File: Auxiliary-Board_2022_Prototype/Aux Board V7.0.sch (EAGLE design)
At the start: 40 parts, among them CON11 1X01, CON12 1X01, CON13 1X01, CON14 1X01, CON15 1X01, CON16 1X01, CON17 1X01, CON18 1X01, CON5 1X01, CON8 1X01

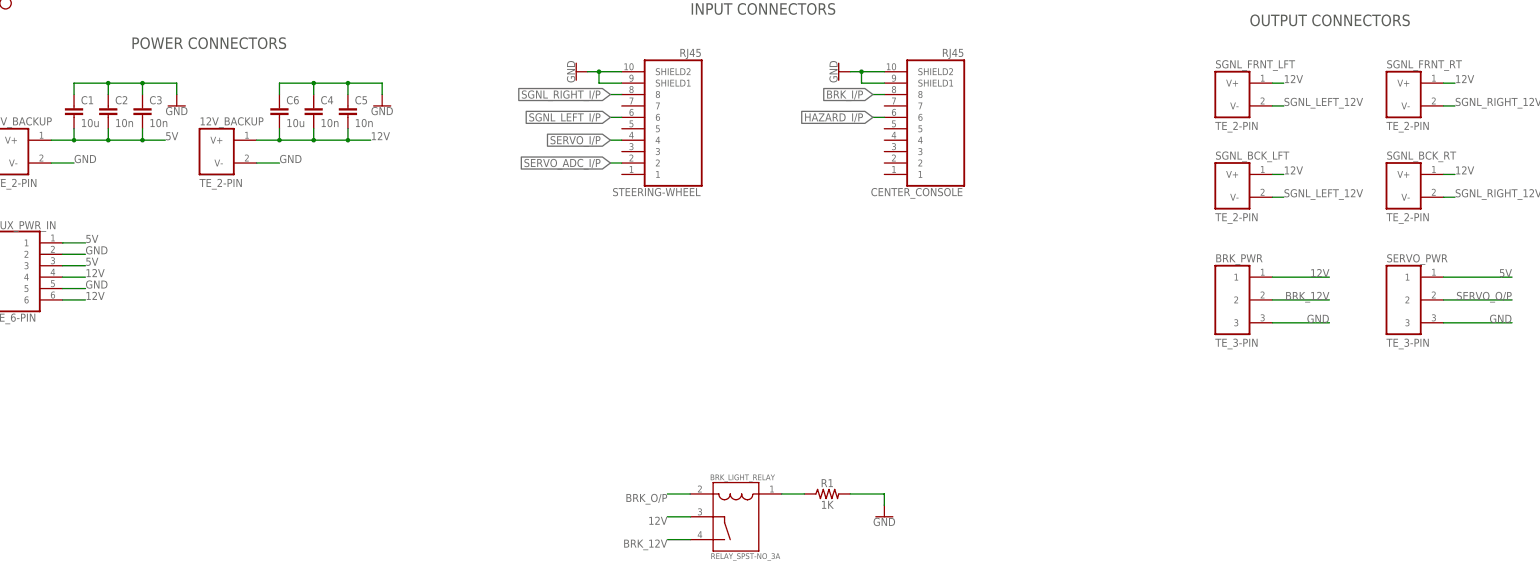
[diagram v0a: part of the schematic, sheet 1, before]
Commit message: feat: rework board, add pwr LEDs, add decoupling caps, add flyback diode
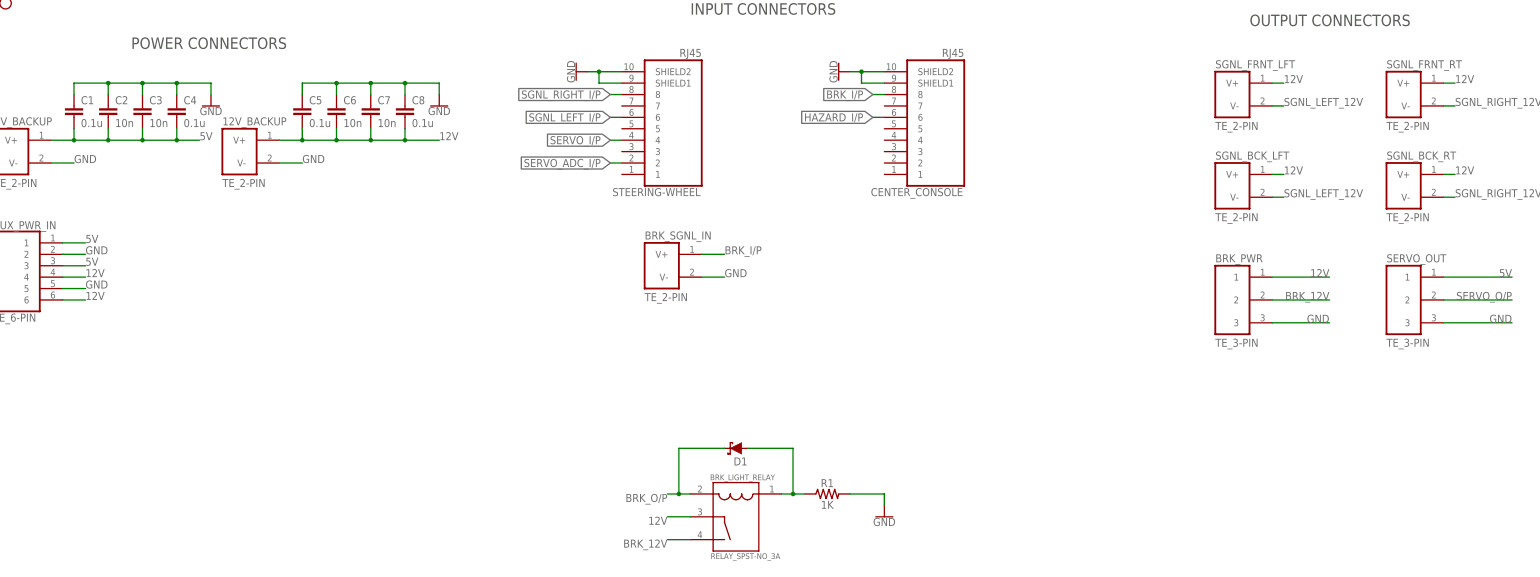
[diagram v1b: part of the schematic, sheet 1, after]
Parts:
- added BRK_SGNL_IN: TE_2-PIN, EcoCar-Connectors:TE_2-PIN
- added C7: 10n, EcoCar-Passives:CAPACITOR_0805
- added C8: 0.1u, EcoCar-Passives:CAPACITOR_0805
- added D1: (no value), EcoCar-Discrete-Semiconductors:DIODE_SCHOTTKY_DO-214AA
- added LED1: (no value), EcoCar-Discrete-Semiconductors:LED_0805
- added R2: 2K, EcoCar-Passives:RESISTOR_0805
- C1: value 10u -> 0.1u
- C4, C5: value 10n -> 0.1u
- C6: value 10u -> 10n
- renumbered SERVO_PWR to SERVO_OUT
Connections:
- new net N$8: LED1.A, R2.1
- net 12V: now also C7.2, C8.2; no longer C4.2
- net 5V: now also C4.2, R2.2
- net BRK_I/P: now also BRK_SGNL_IN.V+, MCU_328P2.PD2(INT0); no longer MCU_328P2.PC1(ADC1)
- net BRK_O/P: now also D1.C
- net GND: now also BRK_SGNL_IN.V-, C7.1, C8.1, LED1.C
- net N$1: now also D1.A
- net SERVO_I/P: now also MCU_328P2.PC1(ADC1); no longer MCU_328P2.PD2(INT0)
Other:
- moved on the sheet: 12V_BACKUP, AVCC_JMP, C4, C5, C6

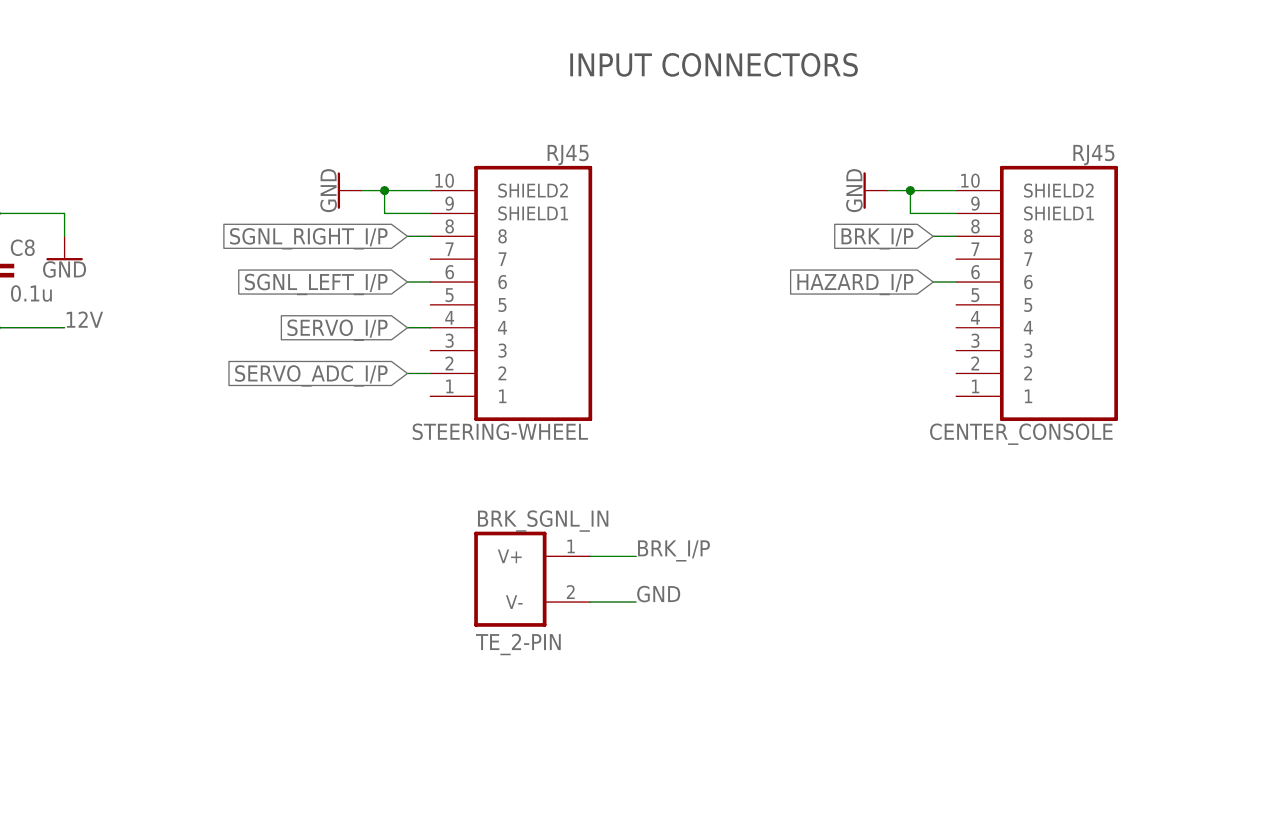
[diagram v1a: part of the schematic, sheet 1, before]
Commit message: feat: add RS232 partially, change inputs to one RJ45 port
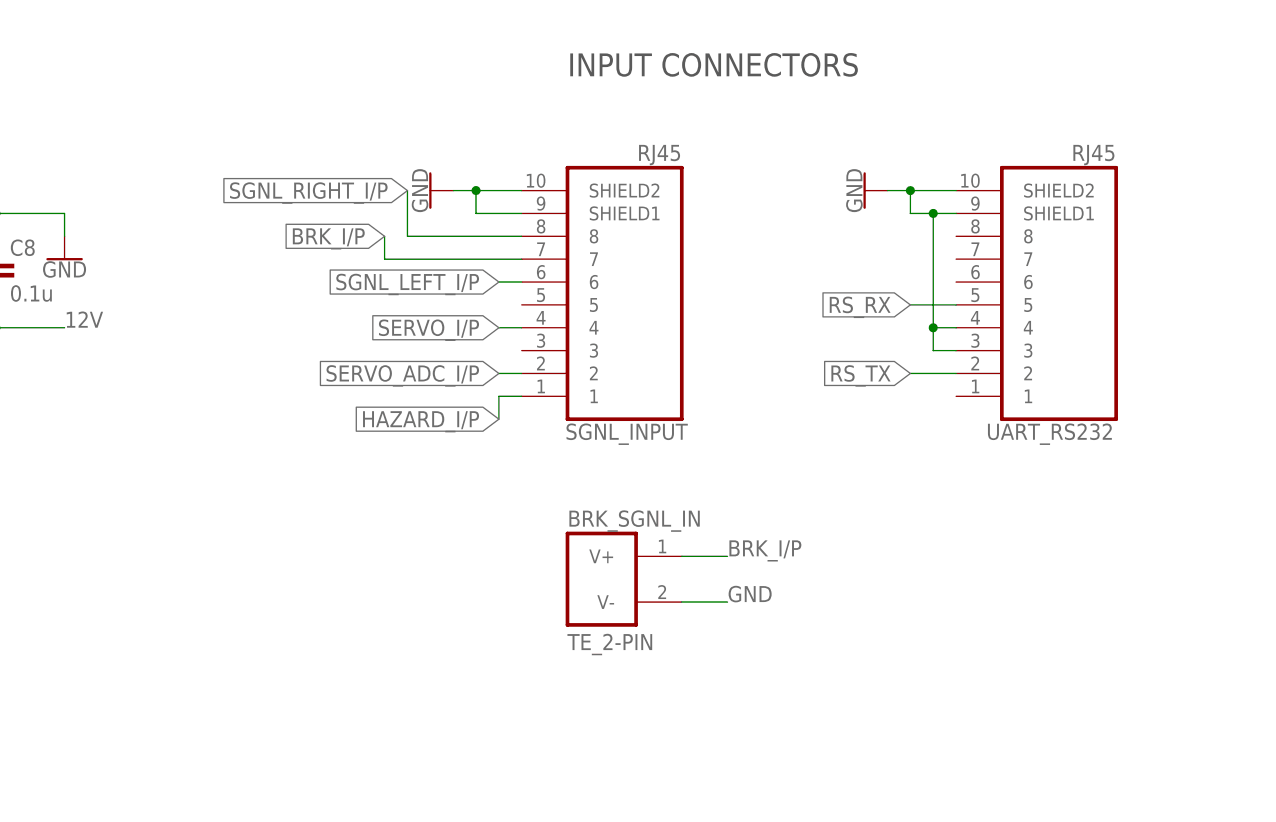
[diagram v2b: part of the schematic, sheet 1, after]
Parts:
- removed STEERING-WHEEL: RJ45, EcoCar-Connectors:RJ45
- added SGNL_INPUT: RJ45, EcoCar-Connectors:RJ45
- renumbered CENTER_CONSOLE to UART_RS232
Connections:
- new net RS_RX: UART_RS232.5
- new net RS_TX: UART_RS232.2
- net BRK_I/P: now also SGNL_INPUT.7; no longer UART_RS232.8
- net GND: now also SGNL_INPUT.SHIELD1, SGNL_INPUT.SHIELD2, UART_RS232.3, UART_RS232.4; no longer STEERING-WHEEL.SHIELD1, STEERING-WHEEL.SHIELD2
- net HAZARD_I/P: now also SGNL_INPUT.1; no longer UART_RS232.6
- net SERVO_ADC_I/P: now also SGNL_INPUT.2; no longer STEERING-WHEEL.2
- net SERVO_I/P: now also SGNL_INPUT.4; no longer STEERING-WHEEL.4
- net SERVO_O/P: now also MCU_328P2.PC5(ADC5/SCL)
- net SGNL_LEFT_I/P: now also SGNL_INPUT.6; no longer STEERING-WHEEL.6
- net SGNL_RIGHT_I/P: now also SGNL_INPUT.8; no longer STEERING-WHEEL.8
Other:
- moved on the sheet: BRK_SGNL_IN

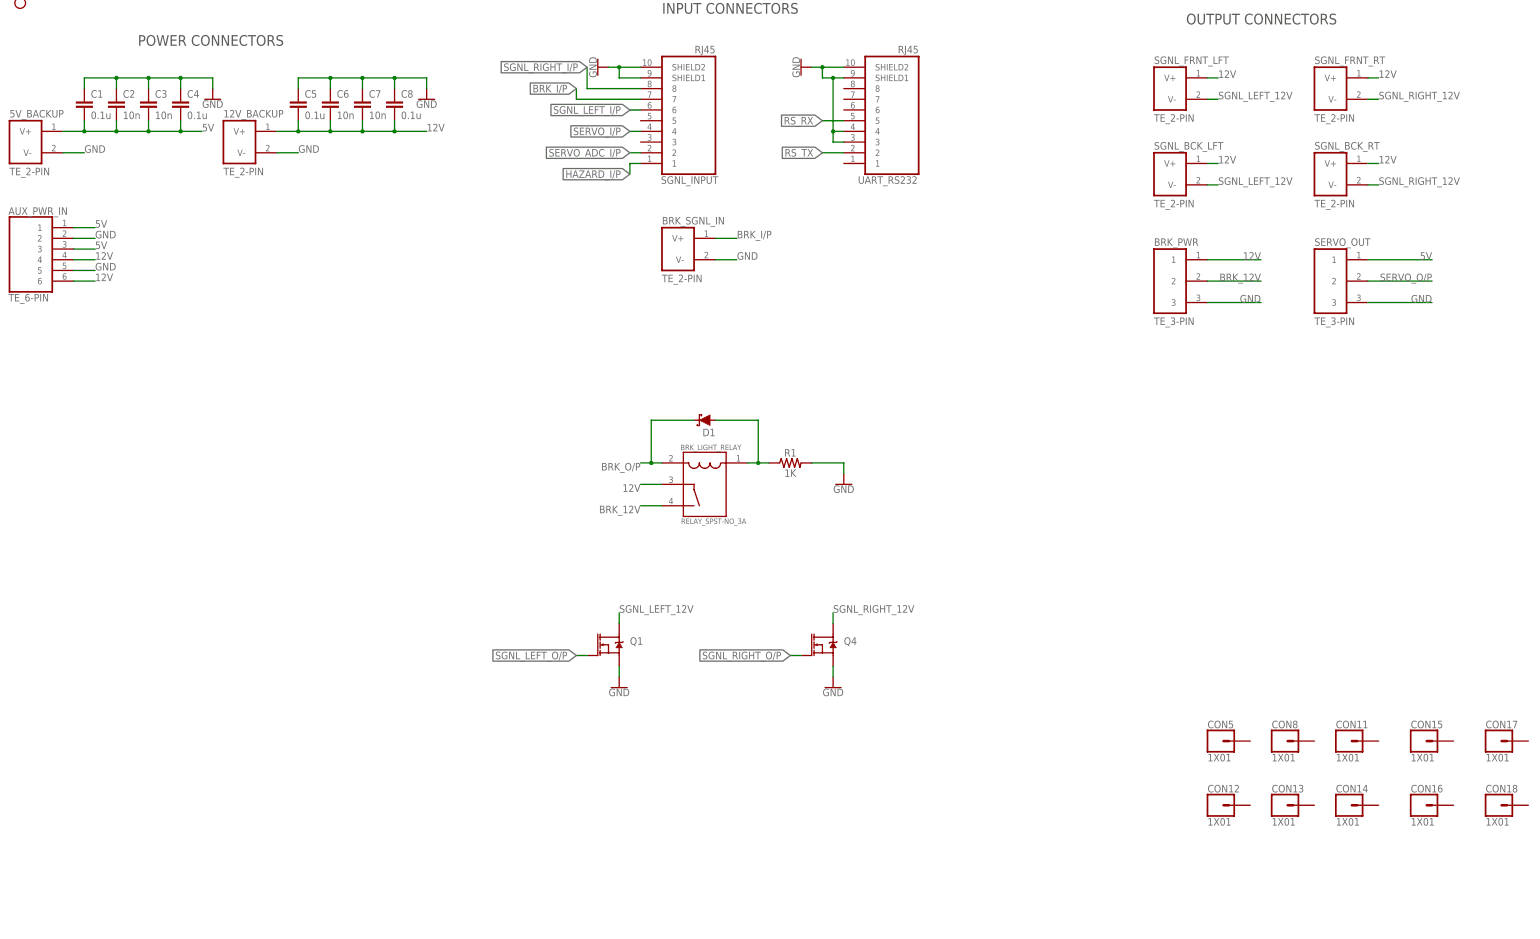
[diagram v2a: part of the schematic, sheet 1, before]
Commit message: feat: converted SGNL switch method from MOSTFETs to Relays
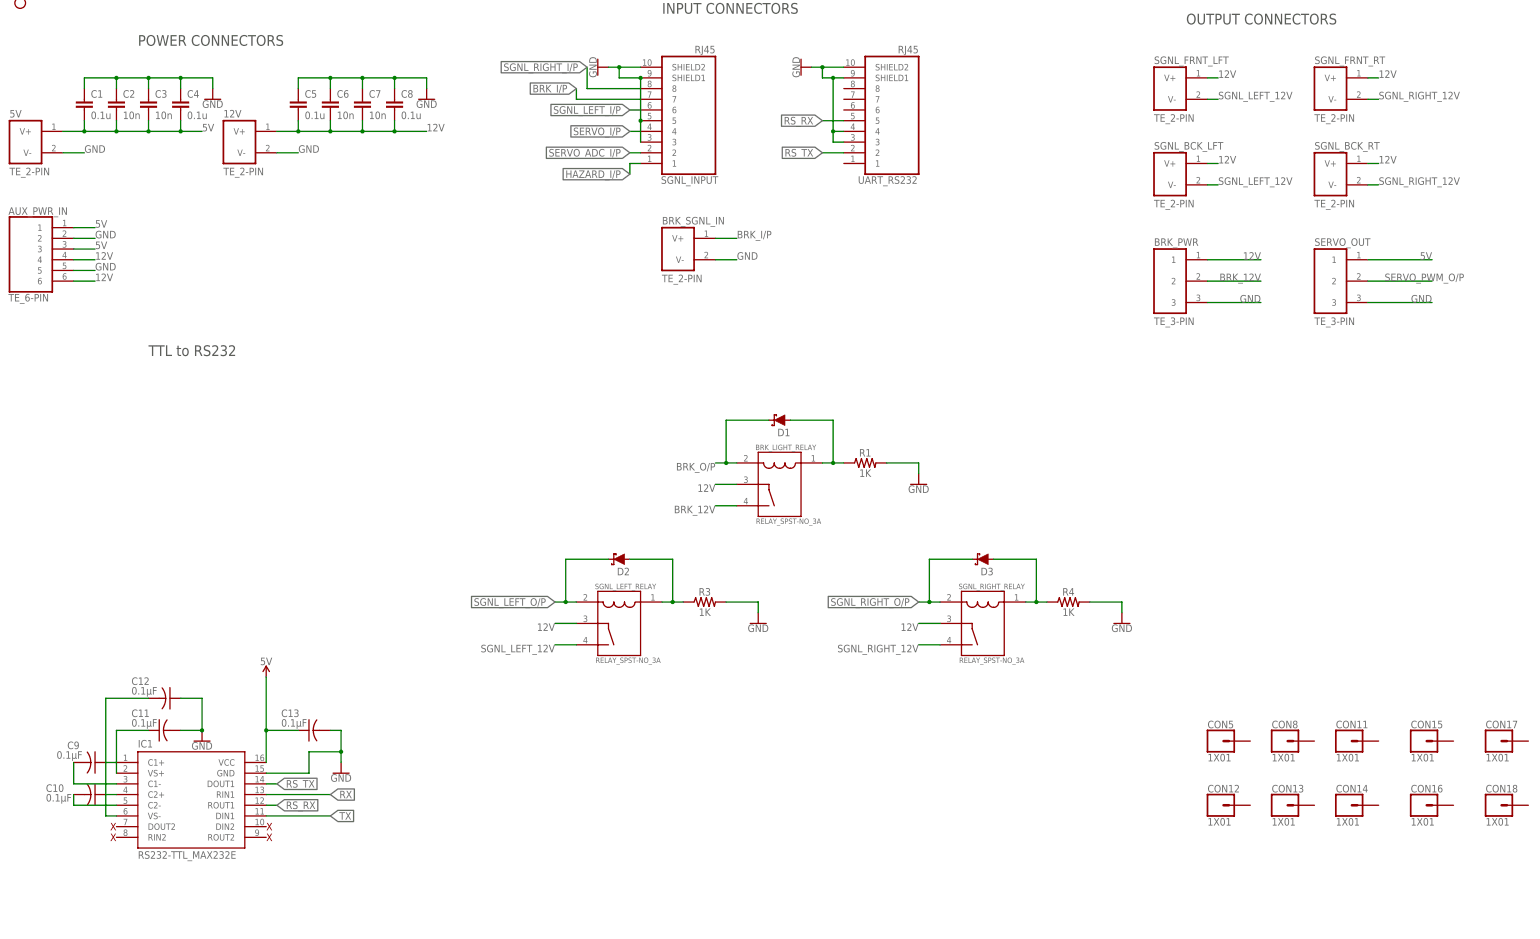
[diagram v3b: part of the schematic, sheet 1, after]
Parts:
- removed Q1, Q4: (no value), EcoCar-Discrete-Semiconductors:MOSFET_NMOS_TO-263
- added C10, C11, C12, C13, C9: 0.1µF, rcl:C-USC0805
- added D2, D3: (no value), EcoCar-Discrete-Semiconductors:DIODE_SCHOTTKY_DO-214AA
- added IC1: RS232-TTL_MAX232E, EcoCar-Integrated-Circuits:RS232-TTL_MAX232E
- added R3, R4: 1K, EcoCar-Passives:RESISTOR_0805
- added SGNL_LEFT_RELAY, SGNL_RIGHT_RELAY: RELAY_SPST-NO_3A, EcoCar-Electromechanical:RELAY_SPST-NO_3A
- renumbered 12V_BACKUP to 12V, 5V_BACKUP to 5V
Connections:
- removed net SERVO_O/P: MCU_328P2.PC5(ADC5/SCL), SERVO_OUT.2
- new net N$10: C10.1, IC1.C2+
- new net N$11: C11.1, IC1.VS+
- new net N$12: C12.2, IC1.VS-
- new net N$13: D2.A, R3.1, SGNL_LEFT_RELAY.1
- new net N$14: D3.A, R4.1, SGNL_RIGHT_RELAY.1
- new net N$6: C9.2, IC1.C1-
- new net N$7: C10.2, IC1.C2-
- new net N$9: C9.1, IC1.C1+
- new net RX: IC1.RIN1, MCU_328P2.PD0(RXD)
- new net SERVO_PWM_O/P: MCU_328P2.PD5(T1), SERVO_OUT.2
- new net TX: IC1.DIN1, MCU_328P2.PD1(TXD)
- net 12V: now also SGNL_LEFT_RELAY.3, SGNL_RIGHT_RELAY.3
- net 5V: now also C13.1, IC1.VCC
- net GND: now also C11.2, C12.1, C13.2, IC1.GND, R3.2, R4.2, SGNL_INPUT.3, SGNL_INPUT.5; no longer Q1.S, Q4.S
- net RS_RX: now also IC1.ROUT1
- net RS_TX: now also IC1.DOUT1
- net SGNL_LEFT_12V: now also SGNL_LEFT_RELAY.4; no longer Q1.D
- net SGNL_LEFT_O/P: now also D2.C, SGNL_LEFT_RELAY.2; no longer Q1.G
- net SGNL_RIGHT_12V: now also SGNL_RIGHT_RELAY.4; no longer Q4.D
- net SGNL_RIGHT_O/P: now also D3.C, SGNL_RIGHT_RELAY.2; no longer Q4.G
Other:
- note added: "TTL to RS232"
- note added: "X"
- moved on the sheet: BRK_LIGHT_RELAY, D1, R1
